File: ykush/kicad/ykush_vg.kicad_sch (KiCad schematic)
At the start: 67 parts, among them J1 USB-C 16P, J2 USB-A port 1, J3 USB-A port 2, J4 USB-A port 3, J5 EXT 5V, J6 PROG/DEBUG, SW1 BOOT, U1 FE1.1s, U2 USBLC6-2SC6, U3 CH552G, U4 SY6280AAC, U5 USBLC6-2SC6, U6 SY6280AAC, U7 USBLC6-2SC6, U8 SY6280AAC, U9 USBLC6-2SC6, Y1 12MHz

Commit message: YKUSH-VG: BOM with Shopee/Lazada, AliExpress, DigiKey and JLCPCB sourcing
- bom.md / bom.csv generated from the schematic, with sourcing per line
- LEDs moved to 0805 green (JLC Basic C2297); bulk caps 220uF
- debug header J6 marked DNP
- check_netlist.py verifies KiCad's netlist against the intended nets

Co-Authored-By: Claude Opus 5.5 <noreply@anthropic.com>
Claude-Session: https://claude.ai/code/session_01EEWbo5vCC8AQXSYmE1aT85
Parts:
- C14, C17, C2, C20: value 150uF -> 220uF
- D3, D4, D5, D6, D7, D8: footprint LED_SMD:LED_0603_1608Metric -> LED_SMD:LED_0805_2012Metric
- J2: value USB-A port 1 -> USB-A port
- J3: value USB-A port 2 -> USB-A port
- J4: value USB-A port 3 -> USB-A port
- J6: now not fitted
- U3: footprint (none) -> Package_SO:SOIC-16_3.9x9.9mm_P1.27mm
- U4, U6, U8: footprint (none) -> Package_TO_SOT_SMD:SOT-23-5

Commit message: YKUSH-VG: move to KiCad 10.0.6, ERC clean
- symbols now come from the KiCad 10 libraries (symdir format), and
  kicad-cli sch upgrade re-saves the schematic in native v10 format
- project file, project symbol library (CH552G, SY6280AAC) and sym-lib-table
- placements snapped to the 2.54 mm grid; USB shield pins renamed to SH (v10)
- screw terminal footprint -> Phoenix MKDS 5.08 (bornier removed in v10)
- kicad-cli sch erc --severity-all: 0 violations; netlist check: 50/50 nets

Co-Authored-By: Claude Opus 5.5 <noreply@anthropic.com>
Claude-Session: https://claude.ai/code/session_01EEWbo5vCC8AQXSYmE1aT85
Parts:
- J5: footprint TerminalBlock:TerminalBlock_bornier-2_P5.08mm -> TerminalBlock_Phoenix:TerminalBlock_Phoenix_MKDS-1,5-2-5.08_1x02_P5.08mm_Horizontal
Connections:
- net GND: now also J1.SH (SHIELD), J2.SH (Shield), J3.SH (Shield), J4.SH (Shield); no longer J1.S1 (SHIELD), J2.5 (Shield), J3.5 (Shield), J4.5 (Shield)

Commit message: YKUSH-VG: layout tooling, Viagrid-aware router, schematic changes for layout, Thailand BOM
- build_pcb.py / placement.py / router.py: build the board with KiCad 10's pcbnew API;
  grid A* router (C core) that only changes layer at the blank's pre-made vias,
  with negotiated-congestion (PathFinder) iterations
- viagrid_9055.json: via map extracted from the official template (it is a ring plus
  clusters, not a full grid); LAYOUT.md documents the constraints and decisions
- schematic: hub port order matched to the board, 0R jumper for the USB-C D+ pads,
  TE 292303-7 SMT USB-A, 22uF per-port bulk, debug header and hub LED dropped,
  XRSTJ/BUSJ tied to the VBUSM divider
- BOM: Shopee/Lazada column now Thailand

Co-Authored-By: Claude Opus 5.5 <noreply@anthropic.com>
Claude-Session: https://claude.ai/code/session_01EEWbo5vCC8AQXSYmE1aT85
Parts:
- removed C14, C17, C20: 220uF, Capacitor_SMD:CP_Elec_6.3x7.7, symbol Device:C_Polarized
- removed C21: 10uF, Capacitor_SMD:C_0805_2012Metric, symbol Device:C
- removed D8: LED_green, LED_SMD:LED_0805_2012Metric, symbol Device:LED
- removed J6: PROG/DEBUG, Connector_PinHeader_2.54mm:PinHeader_1x08_P2.54mm_Vertical, symbol Connector_Generic:Conn_01x08
- removed R18: 10k, Resistor_SMD:R_0603_1608Metric, symbol Device:R
- removed R19: 100k, Resistor_SMD:R_0603_1608Metric, symbol Device:R
- removed R20: 1k, Resistor_SMD:R_0603_1608Metric, symbol Device:R
- added C14, C17: 10uF, Capacitor_SMD:C_0805_2012Metric, symbol Device:C
- added JP1: 0R, Resistor_SMD:R_0603_1608Metric, symbol Device:R
- C12: value 100nF -> 22uF; footprint Capacitor_SMD:C_0603_1608Metric -> Capacitor_SMD:C_1206_3216Metric
- C15, C18: value 10uF -> 22uF; footprint Capacitor_SMD:C_0805_2012Metric -> Capacitor_SMD:C_1206_3216Metric
- C9: value 100nF -> 10uF; footprint Capacitor_SMD:C_0603_1608Metric -> Capacitor_SMD:C_0805_2012Metric
- J2, J3, J4: footprint Connector_USB:USB_A_Molex_67643_Horizontal -> Connector_USB:USB_A_TE_292303-7_Horizontal
- R10: value 10k -> 100k
- R5: value 100k -> 56k
- R6: value 47k -> 100k
- R7: value 100k -> 10k
- R8: value 100k -> 1k
- R9: value 330 -> 10k
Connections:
- net HUB_RSTJ is gone; now on net VBUSM: C8.1, R5.2, U1.17 (~{XRSTJ})
- net +3V3: no longer R5.1, R8.1
- net +5V_PORT: now also C11.1, C14.1, C17.1; no longer C13.1, C16.1, C19.1
- net BOOT_R: now also R7.1; no longer R10.1
- net EN1: now also R10.1; no longer R13.1
- net EN2: now also R13.1; no longer R16.1
- net EN3: now also R16.1
- net GND: now also R10.2, R6.2, R9.2, C14.2, C17.2; no longer R7.2
- net ISET1: now also R9.1; no longer R12.1
- net ISET2: now also R12.1; no longer R15.1
- net ISET3: now also R15.1
- net LED_P1: now also D5.2 (A), R11.2; no longer D6.2 (A), R14.2
- net LED_P2: now also D6.2 (A), R14.2; no longer D7.2 (A), R17.2
- net LED_P3: now also D7.2 (A), R17.2
- net LED_STAT: now also R8.1; no longer R11.1
- net LED_STAT_A: now also D4.2 (A), R8.2; no longer D5.2 (A), R11.2
- net MCU_DP: now also R7.2; no longer R10.2
- net P1_DM: now also U1.6 (DM3); no longer U1.10 (DM1)
- net P1_DP: now also U1.7 (DP3); no longer U1.11 (DP1)
- net P3_DM: now also U1.10 (DM1); no longer U1.6 (DM3)
- net P3_DP: now also U1.11 (DP1); no longer U1.7 (DP3)
- net UP_DP: now also JP1.2; no longer J1.A6 (D+)
- net V33_MCU: now also C10.1; no longer C12.1
- net VBUSM: now also R6.1, U1.19 (BUSJ); no longer C9.1, R6.2, R7.1
- net VBUS_P1: now also C12.1, C13.1, R11.1; no longer C15.1, R14.1
- net VBUS_P2: now also C15.1, C16.1, R14.1; no longer C18.1, R17.1
- net VBUS_P3: now also C18.1, C19.1, R17.1
- net VBUS_UP: now also C9.1, R5.1; no longer C10.1, C11.1, R6.1
- removed net BUSJ: R8.2, U1.19 (BUSJ)
- net HUB_DRV: no longer names the net of U1.22 (DRV)
- net HUB_DRV: no longer R9.1
- removed net LED_HUB: D4.2 (A), R9.2
- net MCU_P14: no longer names the net of U3.2 (P1.4)
- net MCU_P15: no longer names the net of U3.3 (P1.5)
- net MCU_P16: no longer names the net of U3.4 (P1.6)
- net MCU_P17: no longer names the net of U3.5 (P1.7)
- net MCU_RST: no longer names the net of U3.6 (RST)
- net MCU_TXD: no longer names the net of U3.7 (P3.1/TXD)
- new net UP_DP_A: J1.A6 (D+), JP1.1
- no-connect marks 7 -> 14
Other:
- note added: "DOWNSTREAM PORTS: SY6280AAC per port, I_LIM = 6800/R_SET (10k -> ~0.68 A); 22uF + 10uF per port"
- note added: "HUB: Terminus FE1.1s (SSOP-28, 0.635mm). No crystal load caps (internal). DRV/LED pins unused."
- note removed: "DOWNSTREAM PORTS: SY6280AAC per port, I_LIM = 6800/R_SET (10k -> ~0.68 A)"
- note removed: "HUB: Terminus FE1.1s (SSOP-28, 0.635mm). No crystal load caps (internal)."

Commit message: YKUSH-VG: rework USB-C entry (JP1 on D-, VBUS via B.Cu spine, drop upstream ESD), move hub decoupling
Board file is still work in progress (routing run in progress).

Co-Authored-By: Claude Opus 5.5 <noreply@anthropic.com>
Claude-Session: https://claude.ai/code/session_01EEWbo5vCC8AQXSYmE1aT85
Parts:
- removed U2, U5, U7, U9: USBLC6-2SC6, Package_TO_SOT_SMD:SOT-23-6, symbol Power_Protection:USBLC6-2SC6
- removed U3: CH552G, Package_SO:SOIC-16_3.9x9.9mm_P1.27mm, symbol ykush_vg:CH552G
- removed U4, U6, U8: SY6280AAC, Package_TO_SOT_SMD:SOT-23-5, symbol ykush_vg:SY6280AAC
- added U2: CH552G, Package_SO:SOIC-16_3.9x9.9mm_P1.27mm, symbol ykush_vg:CH552G
- added U3, U5, U7: SY6280AAC, Package_TO_SOT_SMD:SOT-23-5, symbol ykush_vg:SY6280AAC
- added U4, U6, U8: USBLC6-2SC6, Package_TO_SOT_SMD:SOT-23-6, symbol Power_Protection:USBLC6-2SC6
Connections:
- net +5V_PORT: now also U3.5 (IN), U5.5 (IN), U7.5 (IN)
- net EN1: now also U2.9 (P1.1), U3.4 (EN)
- net EN2: now also U2.10 (P3.3), U5.4 (EN)
- net EN3: now also U2.11 (P3.4), U7.4 (EN)
- net GND: now also U2.14 (GND), U3.2 (GND), U4.2 (GND), U5.2 (GND), U6.2 (GND), U7.2 (GND), U8.2 (GND)
- net ISET1: now also U3.3 (ISET)
- net ISET2: now also U5.3 (ISET)
- net ISET3: now also U7.3 (ISET)
- net LED_STAT: now also U2.1 (P3.2/INT0)
- net MCU_DM: now also U2.13 (P3.7/UDM)
- net MCU_DP: now also U2.12 (P3.6/UDP)
- net P1_DM: now also U4.3 (I/O2), U4.4 (I/O2)
- net P1_DP: now also U4.1 (I/O1), U4.6 (I/O1)
- net P2_DM: now also U6.3 (I/O2), U6.4 (I/O2)
- net P2_DP: now also U6.1 (I/O1), U6.6 (I/O1)
- net P3_DM: now also U8.3 (I/O2), U8.4 (I/O2)
- net P3_DP: now also U8.1 (I/O1), U8.6 (I/O1)
- net UP_DM: now also JP1.2; no longer J1.A7 (D-)
- net UP_DP: now also J1.A6 (D+); no longer JP1.2
- net V33_MCU: now also U2.16 (V33)
- net VBUS_P1: now also U3.1 (OUT), U4.5 (VBUS)
- net VBUS_P2: now also U5.1 (OUT), U6.5 (VBUS)
- net VBUS_P3: now also U7.1 (OUT), U8.5 (VBUS)
- net VBUS_UP: now also U2.15 (VCC)
- net UP_DP_A renamed UP_DM_A
- net UP_DM_A: now also J1.A7 (D-); no longer J1.A6 (D+)
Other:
- note added: "UPSTREAM USB-C (device/UFP)"
- note removed: "UPSTREAM USB-C (device/UFP) + ESD"

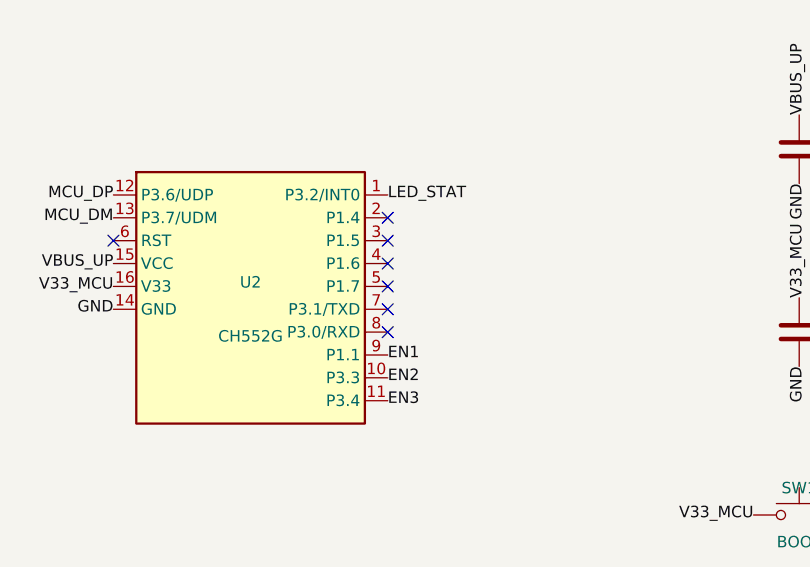
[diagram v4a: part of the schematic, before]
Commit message: Route GND as a net (pads to nearest Viagrid via); finish pass (retry unrouted nets, sync pin changes); EN1 moved to CH552 P1.4; geometric pour-island detection
Co-Authored-By: Claude Opus 5.5 <noreply@anthropic.com>
Claude-Session: https://claude.ai/code/session_01EEWbo5vCC8AQXSYmE1aT85
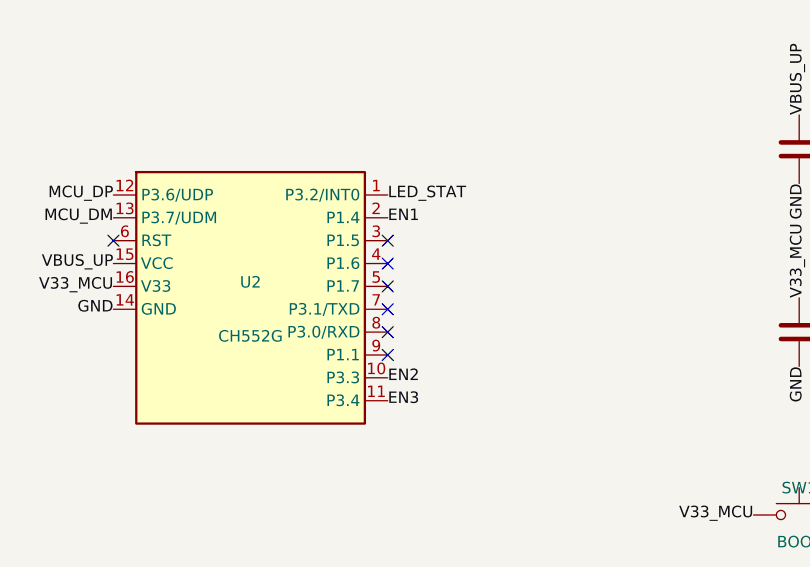
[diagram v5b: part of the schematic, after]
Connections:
- net EN1: now also U2.2 (P1.4); no longer U2.9 (P1.1)
